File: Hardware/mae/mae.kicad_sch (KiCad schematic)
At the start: 34 parts, among them J1 Guitar_IN, J2 POWER_IN, J3 530480310, Q1 Q_NJFET_DSG, U4 NE5532

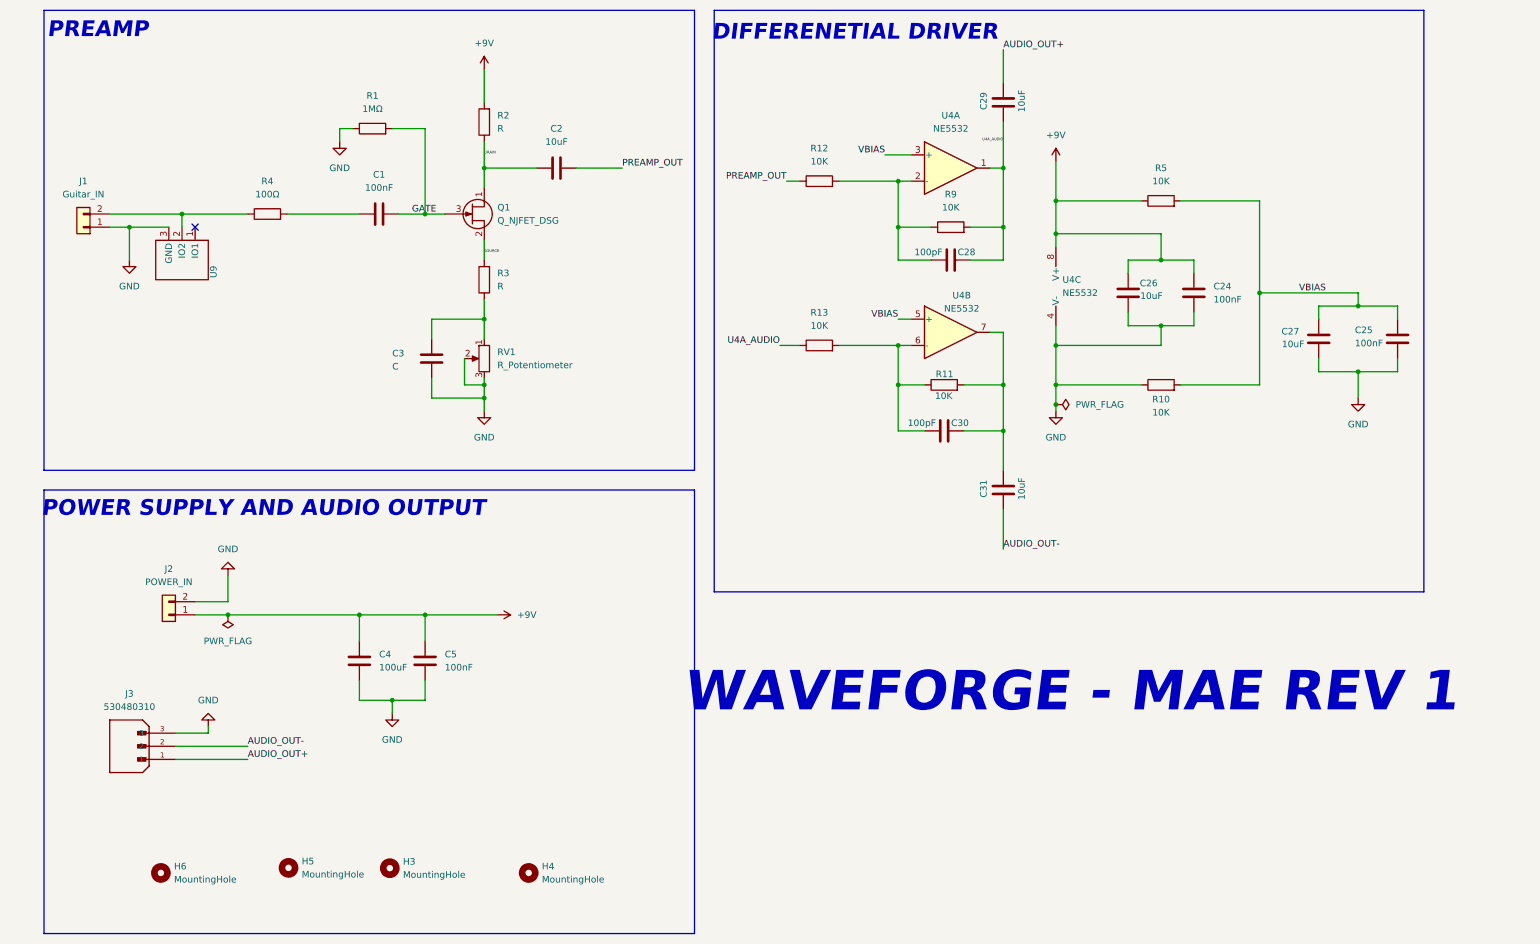
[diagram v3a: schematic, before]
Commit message: Mae: polarised caps, new layout and prints
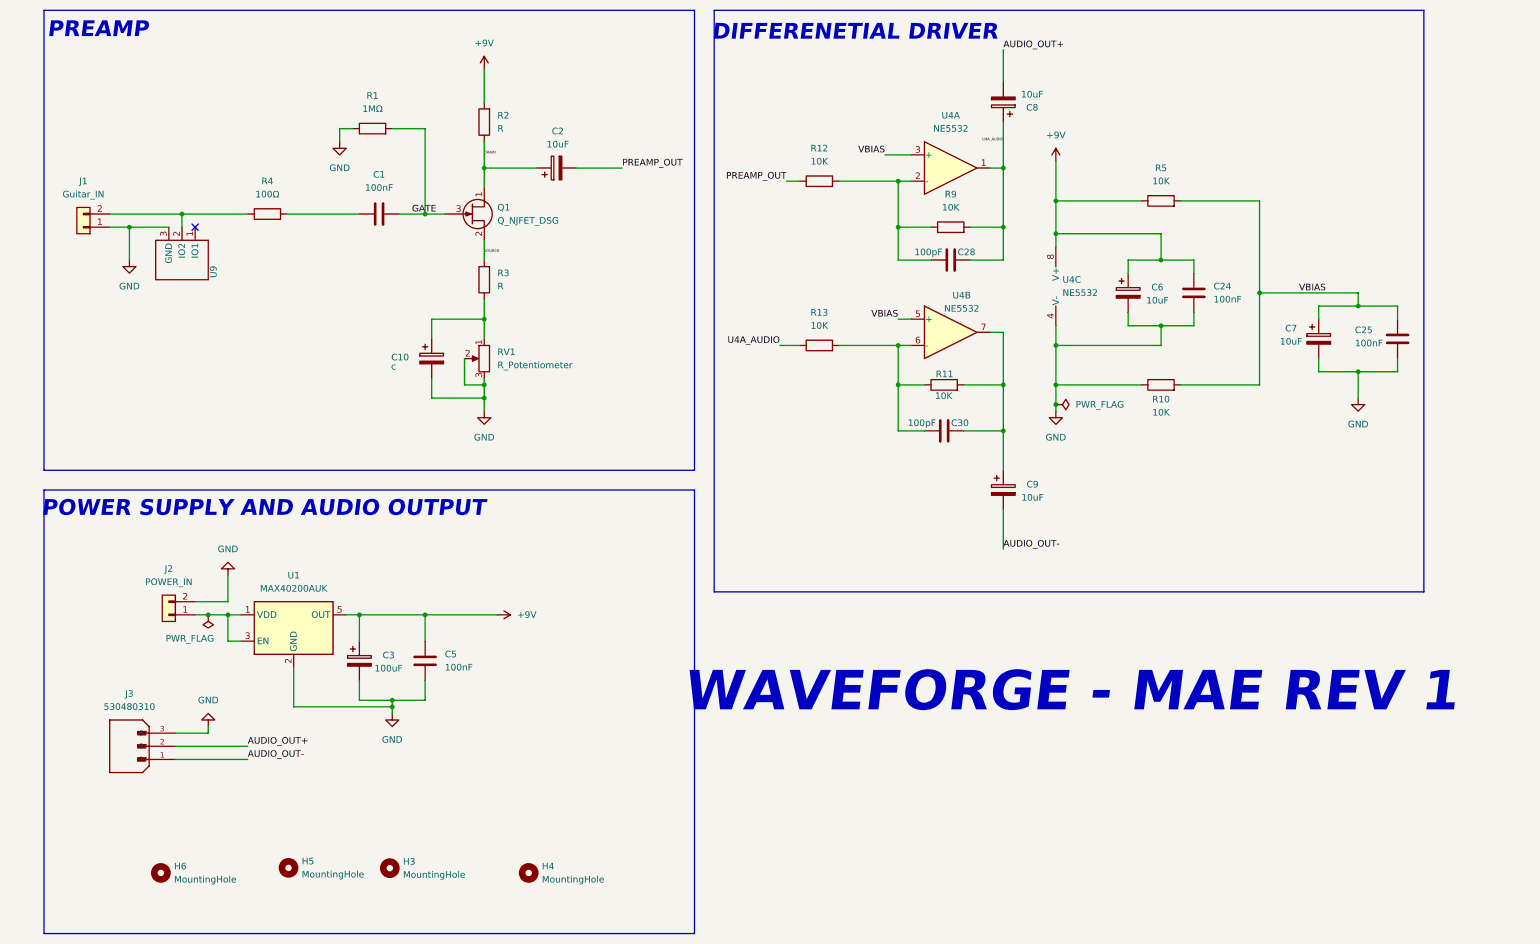
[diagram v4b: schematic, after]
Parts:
- removed C2, C26, C27, C29, C31: 10uF, Capacitor_THT:C_Radial_D5.0mm_H5.0mm_P2.00mm, symbol Device:C
- removed C3: C, Capacitor_THT:C_Radial_D6.3mm_H7.0mm_P2.50mm, symbol Device:C
- removed C4: 100uF, Capacitor_THT:C_Radial_D6.3mm_H7.0mm_P2.50mm, symbol Device:C
- added C10: c, Capacitor_THT:CP_Radial_D6.3mm_P2.50mm, symbol Device:C_Polarized
- added C2, C6, C7, C8, C9: 10uF, Capacitor_THT:CP_Radial_D6.3mm_P2.50mm, symbol Device:C_Polarized
- added C3: 100uF, Capacitor_THT:CP_Radial_D10.0mm_P7.50mm, symbol Device:C_Polarized
- added U1: MAX40200AUK, Package_TO_SOT_SMD:SOT-23-5, symbol Analog_Switch:MAX40200AUK
- C1, C24, C25, C28, C30, C5: footprint Capacitor_THT:C_Disc_D3.0mm_W1.6mm_P2.50mm -> Capacitor_THT:C_Rect_L7.0mm_W2.0mm_P5.00mm
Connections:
- net +9V: now also C3.1, C6.1, U1.5 (OUT); no longer J2.1 (Pin_1)
- net AUDIO_OUT+: now also J3.2, C8.2; no longer J3.1
- net AUDIO_OUT-: now also J3.1, C9.2; no longer J3.2
- net DRAIN: now also C2.1
- net GND: now also C10.2, C3.2, C6.2, C7.2, U1.2 (GND)
- net PREAMP_OUT: now also C2.2
- net U4A_AUDIO: now also C8.1
- net VBIAS: now also C7.1
- net at R3.1, RV1.1: now also C10.1
- net at C30.2, R11.2, U4.7: now also C9.1
- new net: J2.1 (Pin_1), U1.1 (VDD), U1.3 (EN)

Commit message: Gen: PSU, rev 1 schems done, mae and shori orderd
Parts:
- C3: footprint Capacitor_THT:CP_Radial_D10.0mm_P7.50mm -> Capacitor_THT:CP_Radial_D10.0mm_P5.00mm
- RV1: footprint Connector_JST:JST_PH_S2B-PH-K_1x02_P2.00mm_Horizontal -> Connector_JST:JST_PH_S3B-PH-K_1x03_P2.00mm_Horizontal
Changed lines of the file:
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@@
 			)
 		)
-		(property "Footprint" "Connector_JST:JST_PH_S2B-PH-K_1x02_P2.00mm_Horizontal"
+		(property "Footprint" "Connector_JST:JST_PH_S3B-PH-K_1x03_P2.00mm_Horizontal"
 			(at 100.33 82.55 0)
 			(hide yes)
@@
 		(in_pos_files yes)
 		(dnp no)
-		(fields_autoplaced yes)
 		(property "Reference" "C5"
-			(at 92.71 139.6999 0)
+			(at 91.44 139.446 0)
 			(show_name no)
 			(do_not_autoplace no)
@@
 		)
 		(property "Value" "100nF"
-			(at 92.71 142.2399 0)
+			(at 91.44 141.986 0)
 			(show_name no)
 			(do_not_autoplace no)
@@
 			)
 		)
-		(property "Footprint" "Capacitor_THT:CP_Radial_D10.0mm_P7.50mm"
+		(property "Footprint" "Capacitor_THT:CP_Radial_D10.0mm_P5.00mm"
 			(at 77.1652 144.78 0)
 			(hide yes)
